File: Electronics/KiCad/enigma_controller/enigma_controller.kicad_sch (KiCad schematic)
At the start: 33 parts, among them J10 0936263006, J11 Conn_02x05_Odd_Even, J12 Conn_01x02, J13 Conn_01x02, J14 USB_C_Receptacle_PowerOnly_6P, J15 Conn_01x02, J16 Conn_01x02, J17 Conn_01x02, J18 Conn_01x02, J19 Conn_01x02, J20 Conn_01x02, J21 Conn_02x05_Odd_Even, J22 Conn_02x05_Odd_Even, J23 Conn_01x02, J24 Conn_01x02, J3 USB1040-GF-L-B, J4 Conn_01x02, J5 46765-0301, J6 Conn_02x05_Odd_Even, J7 Conn_02x07_Odd_Even, J8 USB3_A_Stacked, J9 Conn_02x07_Odd_Even, M1 Fan_4pin

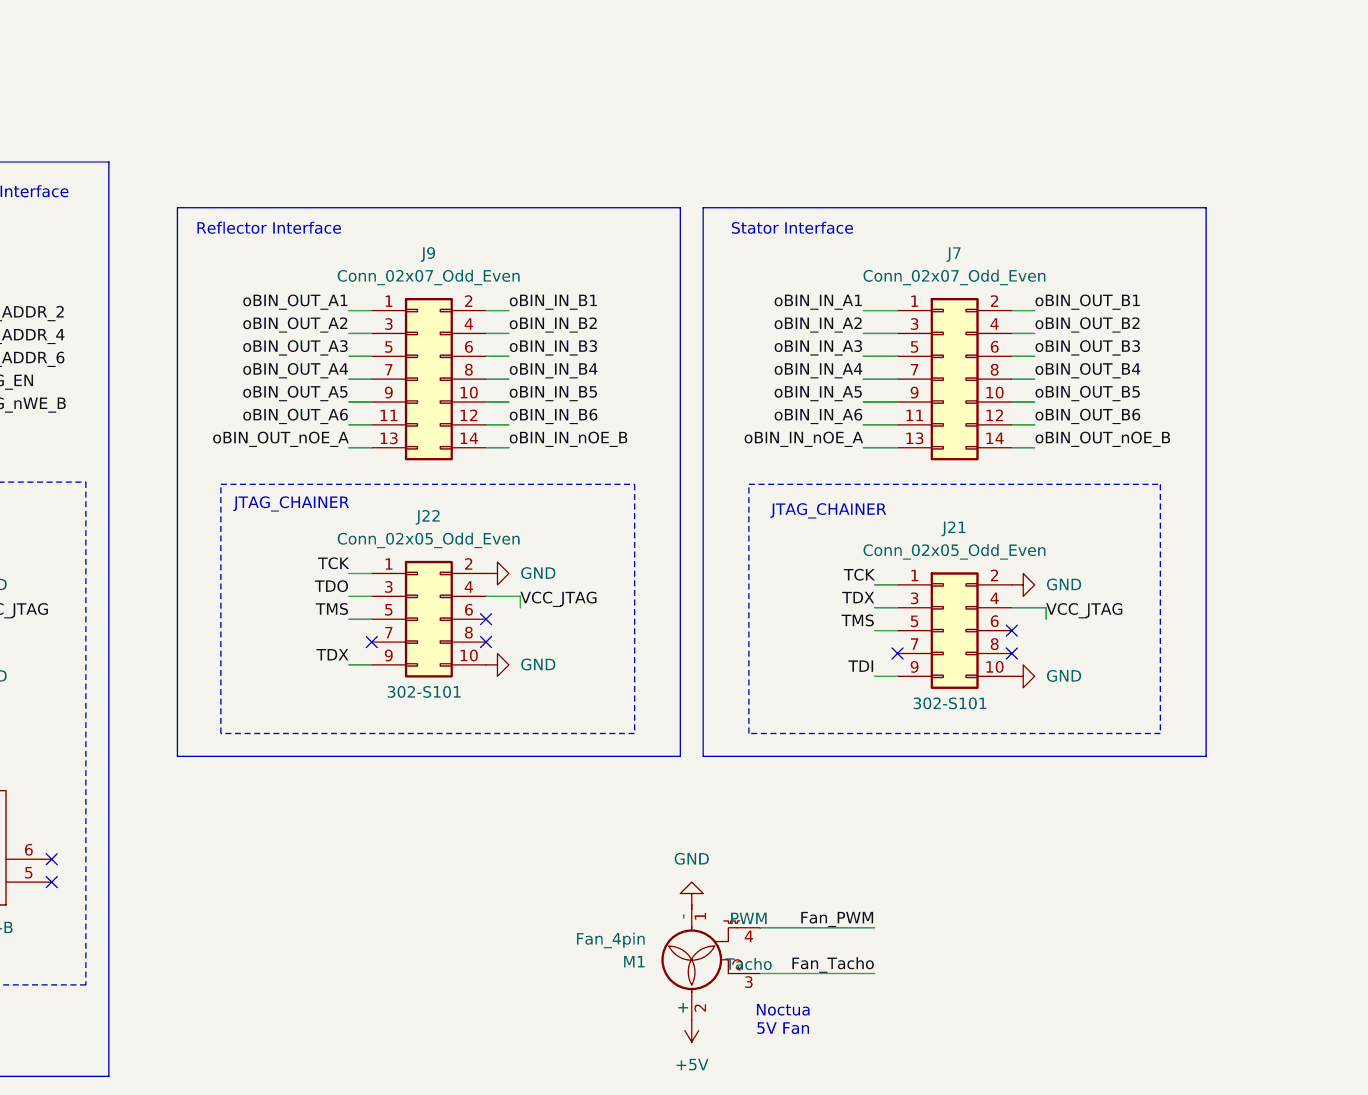
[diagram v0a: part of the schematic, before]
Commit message: Refactored to remove debugger components.
Debug board is now a separate entity.
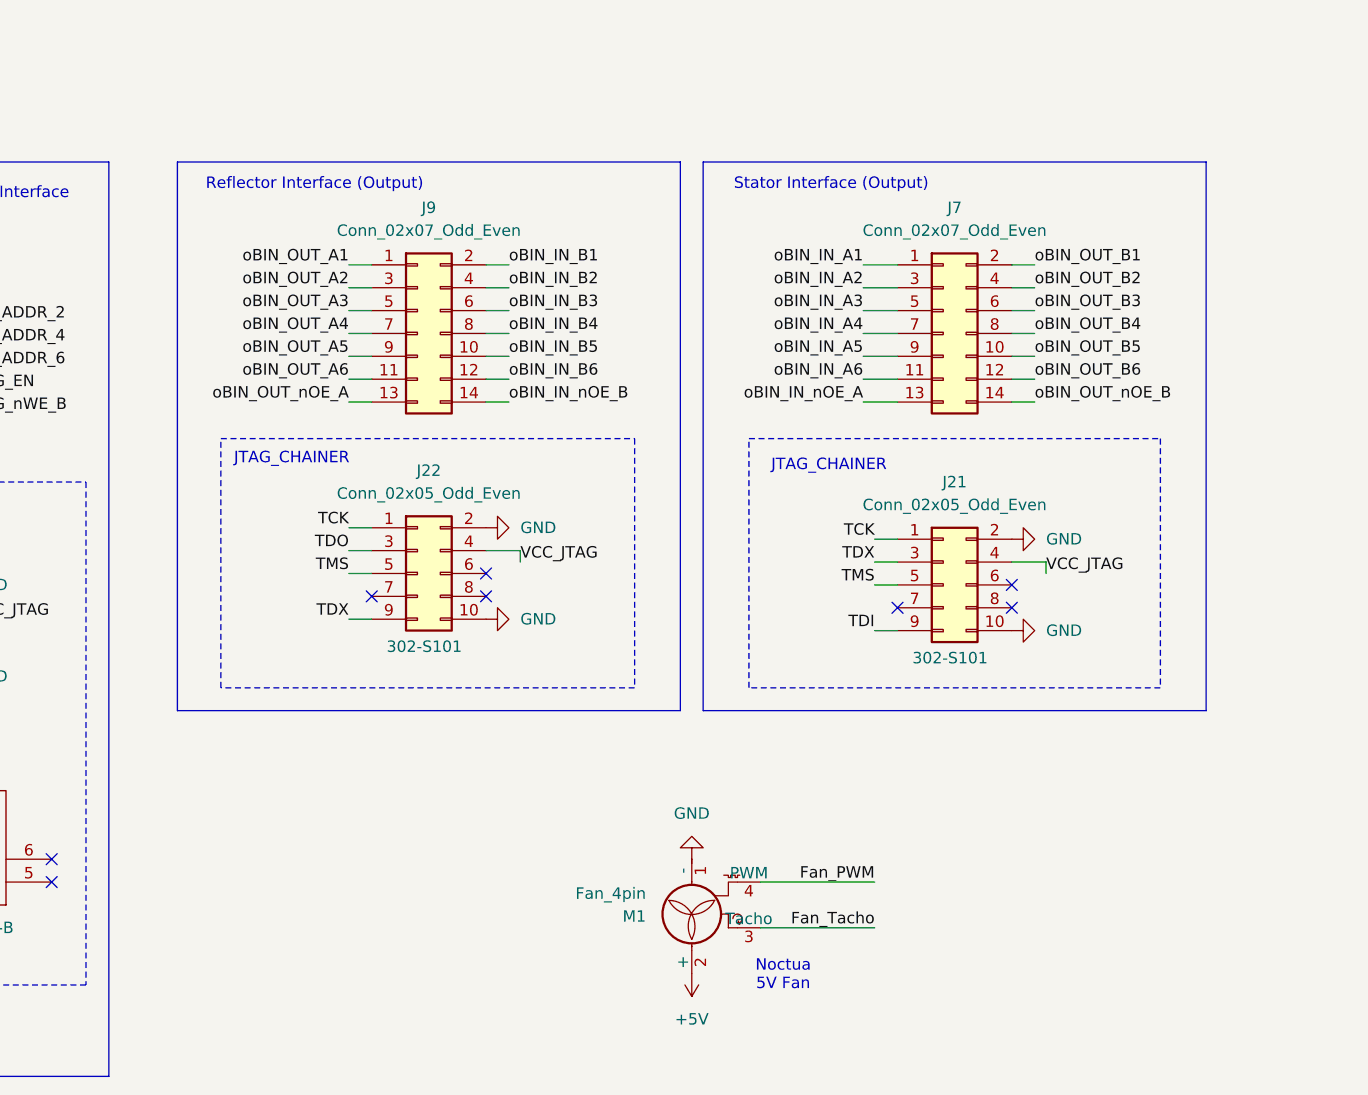
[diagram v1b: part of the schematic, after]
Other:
- note added: "Reflector Interface (Output)"
- note added: "Stator Interface (Output)"
- note removed: "Reflector Interface"
- note removed: "Stator Interface"
- moved on the sheet: J21, J22, J7, J9, M1

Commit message: Updates after TF review.
Added power regulators (CM5IO Schematic source).
Added decoupling caps.
Started replacing custom components with JLCPCB library variants.
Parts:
- removed J12, J13, J4: Conn_01x02, Connector_PinHeader_2.54mm:PinHeader_1x02_P2.54mm_Vertical, symbol Connector_Generic:Conn_01x02
- removed R3, R4: ERA2AEB201X, Enigma_Components:ERA2AED122X, symbol Enigma_Components:ERA2AEB201X
- added C1, C2, C7, C8: 100nF, PCM_JLCPCB:C_0402, symbol PCM_JLCPCB-Capacitors:0402,100nF,(2)
- added C3, C4, C5: CKG57NX7R1H106M500JH, Enigma_Components:CAPC6050X550N, symbol Enigma_Components:CKG57NX7R1H106M500JH
- added C6: CKG57NX7R1E107M500JH, Enigma_Components:CAPC6050X550N, symbol Enigma_Components:CKG57NX7R1E107M500JH
- added H2, H3, H4, H5, H6, H7: MountingHole_Pad, MountingHole:MountingHole_4.3mm_M4_Pad_Via, symbol Mechanical:MountingHole_Pad
- added IC11: RT9742SNGV, Enigma_Components:SOT95P279X130-3N, symbol Enigma_Components:RT9742SNGV
- added IC8: AP22653W6-7, Enigma_Components:SOT95P280X145-6N, symbol Enigma_Components:AP22653W6-7
- added J25, J26, J27: Conn_01x02, Connector_PinHeader_2.54mm:PinHeader_1x02_P2.54mm_Vertical, symbol Connector_Generic:Conn_01x02
- added J28: Conn_02x03_Odd_Even, Connector_PinHeader_2.54mm:PinHeader_2x03_P2.54mm_Vertical, symbol Connector_Generic:Conn_02x03_Odd_Even
- added R3, R4: 470Ω, PCM_JLCPCB:R_0402, symbol PCM_JLCPCB-Resistors:0402,470Ω
- added R5, R6, R7: 2.2kΩ, PCM_JLCPCB:R_0402, symbol PCM_JLCPCB-Resistors:0402,2.2kΩ
- added R8: 10kΩ, PCM_JLCPCB:R_0402, symbol PCM_JLCPCB-Resistors:0402,10kΩ
- added R9: 15kΩ, PCM_JLCPCB:R_0402, symbol PCM_JLCPCB-Resistors:0402,15kΩ
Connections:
- net +3V3: now also J25.1 (Pin_1), J26.1 (Pin_1), J27.1 (Pin_1), R3.2, R4.2, R6.2, R7.1, R8.1; no longer H1.111 (VBUS_EN)
- net +5V: now also C1.1, C2.1, C3.1, C7.1, IC11.1 (VIN), IC8.1 (IN), R5.1; no longer J3.1, J5.19 (+5V_POWER), J8.1 (VBUS1), J8.10 (VBUS2)
- net Fan_PWM: now also R8.2
- net GND: now also S1.1 (COM), S2.1 (COM), C1.2, C2.2, C3.2, C4.2, C5.2, C6.2, C7.2, C8.2, IC11.3 (GND), IC8.2 (GND), J25.2 (Pin_2), J26.2 (Pin_2), J27.2 (Pin_2), J28.1 (Pin_1), J28.3 (Pin_3), J28.5 (Pin_5), R5.2, R9.2
- net SHIELD: now also H2.1, H3.1, H4.1, H5.1, H6.1, H7.1
- net EEPROM_nWP: now reaches H1.20 (EEPROM_nWP)
- net EEPROM_nWP: now also J28.6 (Pin_6)
- net at H1.35 (ID_SC): now also R6.1
- net at H1.36 (ID_SD): now also R7.2
- net WL_nDisable: now reaches H1.89 (WL_nDisable)
- net WL_nDisable: now also J28.4 (Pin_4)
- net BT_nDisable: now reaches H1.91 (BT_nDisable)
- net BT_nDisable: now also J28.2 (Pin_2)
- net at J10.11 (A_GREEN): now also R3.1
- net at J10.13 (A_YELLOW): now also R4.1
- new net: IC8.5 (ILIM), R9.1
- new net HDMI_5V: C8.1, IC11.2 (VOUT), J5.19 (+5V_POWER)
- new net VBUS: C4.1, C5.1, C6.1, IC8.6 (OUT), J3.1, J8.1 (VBUS1), J8.10 (VBUS2)
- new net VBUS_EN: H1.111 (VBUS_EN), IC8.3 (EN)
- no-connect marks 93 -> 90
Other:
- note added: "USB Type-C PD Discharge"
- moved on the sheet: J10, J11, J15, J21, J22, J3, J5, J6, J7, J8A, J8B, J9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

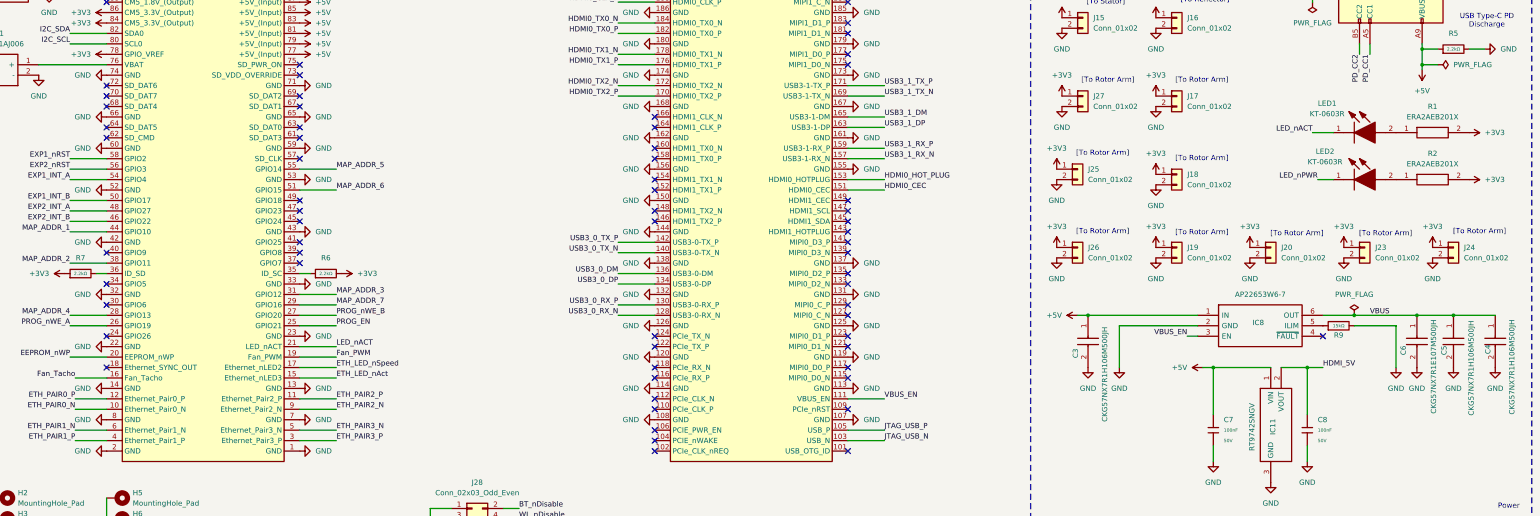
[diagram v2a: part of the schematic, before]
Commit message: Controller updates based on CM5IO board schematics.
Added some extra datasheets.
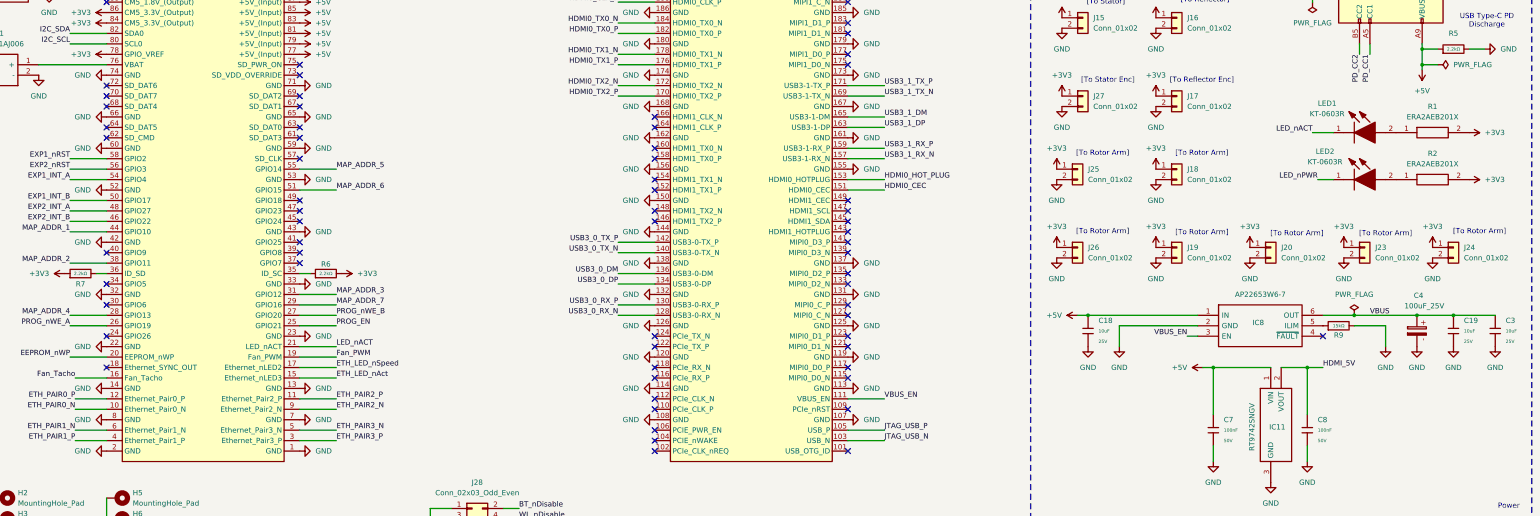
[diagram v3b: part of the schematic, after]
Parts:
- removed C3, C4, C5: CKG57NX7R1H106M500JH, Enigma_Components:CAPC6050X550N, symbol Enigma_Components:CKG57NX7R1H106M500JH
- removed C6: CKG57NX7R1E107M500JH, Enigma_Components:CAPC6050X550N, symbol Enigma_Components:CKG57NX7R1E107M500JH
- added C18, C19, C3: 10uF, PCM_JLCPCB:C_0603, symbol PCM_JLCPCB-Capacitors:0603,10uF,(2)
- added C4: 100uF_25V, Capacitor_THT:CP_Radial_D6.3mm_P2.50mm, symbol PCM_SL_Capacitors:100uF_25V
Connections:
- net +5V: now also C18.1
- net GND: now also C18.2, C19.2, C3.2, C4.2
- net VBUS: now also C19.1, C3.1, C4.1
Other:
- note added: "[To Reflector Enc]"
- note added: "[To Stator Enc]"
- moved on the sheet: J18

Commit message: Added ESD Protection.
Also updated some components to follow reference CM5IO board.
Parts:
- removed C18, C19, C3: 10uF, PCM_JLCPCB:C_0603, symbol PCM_JLCPCB-Capacitors:0603,10uF,(2)
- removed C4: 100uF_25V, Capacitor_THT:CP_Radial_D6.3mm_P2.50mm, symbol PCM_SL_Capacitors:100uF_25V
- removed C7, C8: 100nF, PCM_JLCPCB:C_0402, symbol PCM_JLCPCB-Capacitors:0402,100nF,(2)
- removed unit 2 of H1
- removed H5, H6, H7: MountingHole_Pad, MountingHole:MountingHole_4.3mm_M4_Pad_Via, symbol Mechanical:MountingHole_Pad
- removed IC11: RT9742SNGV, Enigma_Components:SOT95P279X130-3N, symbol Enigma_Components:RT9742SNGV
- removed IC8: AP22653W6-7, Enigma_Components:SOT95P280X145-6N, symbol Enigma_Components:AP22653W6-7
- removed J10: 0936263006, Enigma_Components:0936263006, symbol Enigma_Components:0936263006
- removed J14: USB_C_Receptacle_PowerOnly_6P, Connector_USB:USB_C_Receptacle_GCT_USB4135-GF-A_6P_TopMnt_Horizontal, symbol Connector:USB_C_Receptacle_PowerOnly_6P
- removed J28: Conn_02x03_Odd_Even, Connector_PinHeader_2.54mm:PinHeader_2x03_P2.54mm_Vertical, symbol Connector_Generic:Conn_02x03_Odd_Even
- removed J5: 46765-0301, Enigma_Components:467650301, symbol Enigma_Components:46765-0301
- removed J8: USB3_A_Stacked, Connector_USB:USB3_A_Molex_48406-0001_Horizontal_Stacked, symbol Connector:USB3_A_Stacked
- removed R1, R2: ERA2AEB201X, Enigma_Components:ERA2AED122X, symbol Enigma_Components:ERA2AEB201X
- removed R3, R4: 470Ω, PCM_JLCPCB:R_0402, symbol PCM_JLCPCB-Resistors:0402,470Ω
- removed R5: 2.2kΩ, PCM_JLCPCB:R_0402, symbol PCM_JLCPCB-Resistors:0402,2.2kΩ
- removed R9: 15kΩ, PCM_JLCPCB:R_0402, symbol PCM_JLCPCB-Resistors:0402,15kΩ
- removed S2: B3U-1100PM, Enigma_Components:B3U1100PM, symbol Enigma_Components:B3U-1100PM
- added C11, C12, C5, C6: 4.7uF 50V, Capacitor_THT:CP_Radial_D5.0mm_P2.00mm, symbol PCM_SL_Capacitors:4.7uF_50V
- added C13: 2.2uF, PCM_JLCPCB:C_1206, symbol PCM_JLCPCB-Capacitors:1206,2.2uF
- added C14: CL21B105KAFNNNG, Enigma_Components:CAPC2012X135N, symbol Enigma_Components:CL21B105KAFNNNG
- added C15, C16, C9: 100nF, PCM_JLCPCB:C_0402, symbol PCM_JLCPCB-Capacitors:0402,100nF,(2)
- added D1, D2: ESD441DPLR, Enigma_Components:ESD441DPLR, symbol Enigma_Components:ESD441DPLR
- added H2: MountingHole_Pad, MountingHole:MountingHole_4.3mm_M4_Pad_Via, symbol Mechanical:MountingHole_Pad
- added H6, H7: MountingHole, MountingHole:MountingHole_4.3mm_M4, symbol Mechanical:MountingHole
- added IC1: TPD8S300ARUKR, Enigma_Components:QFN40P300X300X80-21N-D, symbol Enigma_Components:TPD8S300ARUKR
- added IC10, IC9: MCP23017-E_SO, Enigma_Components:SOIC127P1030X265-28N, symbol Enigma_Components:MCP23017-E_SO
- added IC2, IC3: ESD321DYAR, Enigma_Components:SODFL1608X77N, symbol Enigma_Components:ESD321DYAR
- added J1: Conn_02x05_Odd_Even, Connector_IDC:IDC-Header_2x05_P2.54mm_Vertical, symbol Connector_Generic:Conn_02x05_Odd_Even
- added J12: Conn_01x02, Connector_PinHeader_2.54mm:PinHeader_1x02_P2.54mm_Vertical, symbol Connector_Generic:Conn_01x02
- added J2: Conn_02x04_Odd_Even, Connector_PinHeader_2.54mm:PinHeader_2x04_P2.54mm_Vertical, symbol Connector_Generic:Conn_02x04_Odd_Even
- added J4: USB_C_Receptacle_USB2.0_16P, Connector_USB:USB_C_Receptacle_Amphenol_124019772112A, symbol Connector:USB_C_Receptacle_USB2.0_16P
- added LED87: KT-0603R, Enigma_Components:LEDC1608X70N, symbol Enigma_Components:KT-0603R
- added R1, R2: 470Ω, PCM_JLCPCB:R_0402, symbol PCM_JLCPCB-Resistors:0402,470Ω
- added R10: 1kΩ, PCM_JLCPCB:R_0402, symbol PCM_JLCPCB-Resistors:0402,1kΩ
- added R11, R12, R13, R14: RCA06030000ZSEA, Enigma_Components:RESC1608X50N, symbol Enigma_Components:RCA06030000ZSEA
- added R5: 100kΩ, PCM_JLCPCB:R_0402, symbol PCM_JLCPCB-Resistors:0402,100kΩ
- renumbered H2 to H3, H3 to H4, H4 to H5
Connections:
- net +3V3: now also C11.1, C12.1, C14.2, C15.1, IC1.10 (VPWR), IC10.15 (A0), IC10.9 (VDD), IC9.9 (VDD), J12.1 (Pin_1), R1.2, R2.2, R5.1
- net +5V: now also C13.1, C5.1, C6.1, C9.1, D1.1, J4.A4 (VBUS), J4.A9 (VBUS), J4.B4 (VBUS), J4.B9 (VBUS)
- net BT_nDisable: now also J2.2 (Pin_2)
- net EEPROM_nWP: now also J2.6 (Pin_6)
- net EXP1_INT_A: now also IC9.20 (INTA)
- net EXP1_INT_B: now also IC9.19 (INTB)
- net EXP1_nRST: now also IC9.18 (~{RESET})
- net EXP2_INT_A: now also IC10.20 (INTA)
- net EXP2_INT_B: now also IC10.19 (INTB)
- net EXP2_nRST: now also IC10.18 (~{RESET})
- net GND: now also C11.2, C12.2, C13.2, C14.1, C16.1, C5.2, C6.2, C9.2, D1.2, D2.2, IC1.13 (GND_2), IC1.18 (GND_3), IC1.21 (EP), IC1.6 (RPD_G2), IC1.7 (RPD_G1), IC1.8 (GND_1), IC10.10 (VSS), IC10.16 (A1), IC10.17 (A2), IC2.1 (GND), IC3.1 (GND), IC9.10 (VSS), IC9.15 (A0), IC9.16 (A1), IC9.17 (A2), J1.10 (Pin_10), J1.2 (Pin_2), J12.2 (Pin_2), J2.1 (Pin_1), J2.3 (Pin_3), J2.5 (Pin_5), J2.7 (Pin_7), J4.A1 (GND), J4.A12 (GND), J4.B1 (GND), J4.B12 (GND), LED87.1
- net I2C_SCL: now also IC10.12 (SCL), IC9.12 (SCL)
- net I2C_SDA: now also IC10.13 (SDA), IC9.13 (SDA)
- net JTAG_USB_N: now also IC3.2 (IO), R13.2
- net JTAG_USB_P: now also IC2.2 (IO), R11.2
- net PD_CC1: now also IC1.12 (CC1)
- net PD_CC2: now also IC1.11 (CC2)
- net PROG_EN: now also R10.2
- net SHIELD: now also J3.5 (MH1), J3.6 (MH2), H2.1, J4.S1 (SHIELD)
- net TCK: now also J1.1 (Pin_1)
- net TDI: now also J22.9 (Pin_9); no longer J21.9 (Pin_9)
- net TDO: now also J1.3 (Pin_3); no longer J22.3 (Pin_3)
- net TMS: now also J1.5 (Pin_5)
- net VBUS: now also C16.2, D2.1
- net VCC_JTAG: now also J1.4 (Pin_4)
- net WL_nDisable: now also J2.4 (Pin_4)
- net nRPIBOOT: now reaches H1.93 (nRPIBOOT)
- net nRPIBOOT: now also J2.8 (Pin_8)
- net at LED1.2: now also R1.1
- net at LED2.2: now also R2.1
- net TDX renamed TDX2
- net TDX2: now also J1.9 (Pin_9); no longer J22.9 (Pin_9)
- net oBIN_IN_A1 renamed pBIN_IN_A1
- net pBIN_IN_A1: now also IC9.1 (GPB0)
- net oBIN_IN_A2 renamed pBIN_IN_A2
- net pBIN_IN_A2: now also IC9.2 (GPB1)
- net oBIN_IN_A3 renamed pBIN_IN_A3
- net pBIN_IN_A3: now also IC9.3 (GPB2)
- net oBIN_IN_A4 renamed pBIN_IN_A4
- net pBIN_IN_A4: now also IC9.4 (GPB3)
- net oBIN_IN_A5 renamed pBIN_IN_A5
- net pBIN_IN_A5: now also IC9.5 (GPB4)
- net oBIN_IN_A6 renamed pBIN_IN_A6
- net pBIN_IN_A6: now also IC9.6 (GPB5)
- net oBIN_IN_B1 renamed pBIN_IN_B1
- net pBIN_IN_B1: now also IC10.1 (GPB0)
- net oBIN_IN_B2 renamed pBIN_IN_B2
- net pBIN_IN_B2: now also IC10.2 (GPB1)
- net oBIN_IN_B3 renamed pBIN_IN_B3
- net pBIN_IN_B3: now also IC10.3 (GPB2)
- net oBIN_IN_B4 renamed pBIN_IN_B4
- net pBIN_IN_B4: now also IC10.4 (GPB3)
- net oBIN_IN_B5 renamed pBIN_IN_B5
- net pBIN_IN_B5: now also IC10.5 (GPB4)
- net oBIN_IN_B6 renamed pBIN_IN_B6
- net pBIN_IN_B6: now also IC10.6 (GPB5)
- net oBIN_IN_nOE_A renamed pBIN_IN_nOE_A
- net pBIN_IN_nOE_A: now also IC9.7 (GPB6)
- net oBIN_IN_nOE_B renamed pBIN_IN_nOE_B
- net pBIN_IN_nOE_B: now also IC10.7 (GPB6)
- net oBIN_OUT_A1 renamed pBIN_OUT_A1
- net pBIN_OUT_A1: now also IC9.21 (GPA0)
- net oBIN_OUT_A2 renamed pBIN_OUT_A2
- net pBIN_OUT_A2: now also IC9.22 (GPA1)
- net oBIN_OUT_A3 renamed pBIN_OUT_A3
- net pBIN_OUT_A3: now also IC9.23 (GPA2)
- net oBIN_OUT_A4 renamed pBIN_OUT_A4
- net pBIN_OUT_A4: now also IC9.24 (GPA3)
- net oBIN_OUT_A5 renamed pBIN_OUT_A5
- net pBIN_OUT_A5: now also IC9.25 (GPA4)
- net oBIN_OUT_A6 renamed pBIN_OUT_A6
- net pBIN_OUT_A6: now also IC9.26 (GPA5)
- net oBIN_OUT_B1 renamed pBIN_OUT_B1
- net pBIN_OUT_B1: now also IC10.21 (GPA0)
- net oBIN_OUT_B2 renamed pBIN_OUT_B2
- net pBIN_OUT_B2: now also IC10.22 (GPA1)
- net oBIN_OUT_B3 renamed pBIN_OUT_B3
- net pBIN_OUT_B3: now also IC10.23 (GPA2)
- net oBIN_OUT_B4 renamed pBIN_OUT_B4
- net pBIN_OUT_B4: now also IC10.24 (GPA3)
- net oBIN_OUT_B5 renamed pBIN_OUT_B5
- net pBIN_OUT_B5: now also IC10.25 (GPA4)
- net oBIN_OUT_B6 renamed pBIN_OUT_B6
- net pBIN_OUT_B6: now also IC10.26 (GPA5)
- net oBIN_OUT_nOE_A renamed pBIN_OUT_nOE_A
- net pBIN_OUT_nOE_A: now also IC9.27 (GPA6)
- net oBIN_OUT_nOE_B renamed pBIN_OUT_nOE_B
- net pBIN_OUT_nOE_B: now also IC10.27 (GPA6)
- new net: C15.2, IC1.3 (VBIAS)
- new net: IC1.9 (~{FLT}), R5.2
- new net: LED87.2, R10.1
- new net C_CC1: IC1.4 (C_CC1), J4.A5 (CC1)
- new net C_CC2: IC1.5 (C_CC2), J4.B5 (CC2)
- new net C_D+: IC1.1 (C_SBU1), J4.A6 (D+), J4.B6 (D+)
- new net C_D-: IC1.2 (C_SBU2), J4.A7 (D-), J4.B7 (D-)
- new net FLASH_D+: IC1.14 (SBU2), R12.2
- new net FLASH_D-: IC1.15 (SBU1), R14.2
- new net TDX1: J21.9 (Pin_9), J22.3 (Pin_3)
- new net USB_DN: R13.1, R14.1
- new net USB_DP: R11.1, R12.1
- no-connect marks 90 -> 54
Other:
- removed sheet enigma_controller_prog
- added sheet enigma_controller_HS (enigma_controller_HS.kicad_sch)
- note added: "Decoupling Caps"
- note added: "JTAG"
- note added: "JTAG_CHAINER (IN-OUT)"
- note added: "JTAG_CHAINER (PLUG1)"
- note added: "JTAG_CHAINER (PLUG2)"
- note added: "JTAG_CHAINER (PROG)"
- note added: "Programmer Interface"
- note added: "Programmer Pins"
- note added: "[To Plugboard 1 Enc]"
- note added: "[To Plugboard 2 Enc]"
- note removed: "JTAG_CHAINER"
- note removed: "Programming Interface"
- note removed: "USB Type-C PD Discharge"
- note removed: "[To Reflector Enc]"
- moved on the sheet: BT1, C1, C2, H1A, H3, H4, H5, J11, J15, J16, J17, J18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
